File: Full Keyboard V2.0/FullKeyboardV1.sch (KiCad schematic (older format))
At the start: 210 parts, among them SW1 Esc, SW10 2, SW11 W, SW12 S, SW13 Z, SW15 3, SW16 E, SW17 D, SW18 X, SW19 4, SW2 Tab, SW20 R, SW21 F, SW22 C, SW23 5, SW24 T, SW25 G, SW26 V, SW27 6, SW28 Y, SW29 H, SW3 Caps, SW30 B, SW32 7, SW33 U, SW34 J, SW35 N, SW36 8, SW37 I, SW38 K, SW39 M, SW4 double_key, SW40 9, SW41 O, SW42 L, SW43 <, SW44 0, SW45 P, SW46 ;, SW47 >, SW49 Minus, SW5 End/Home, SW50 [, SW51 \", SW52 /, SW54 =, SW55 ], SW59 BKSPC, SW6 1, SW60 \\, SW61 Enter, SW63 Til, SW64 Del, SW65 Pg Up, SW66 Pg Dw, SW7 Q, SW8 A, SW9 double_key, U5 Cherry_bottom_row

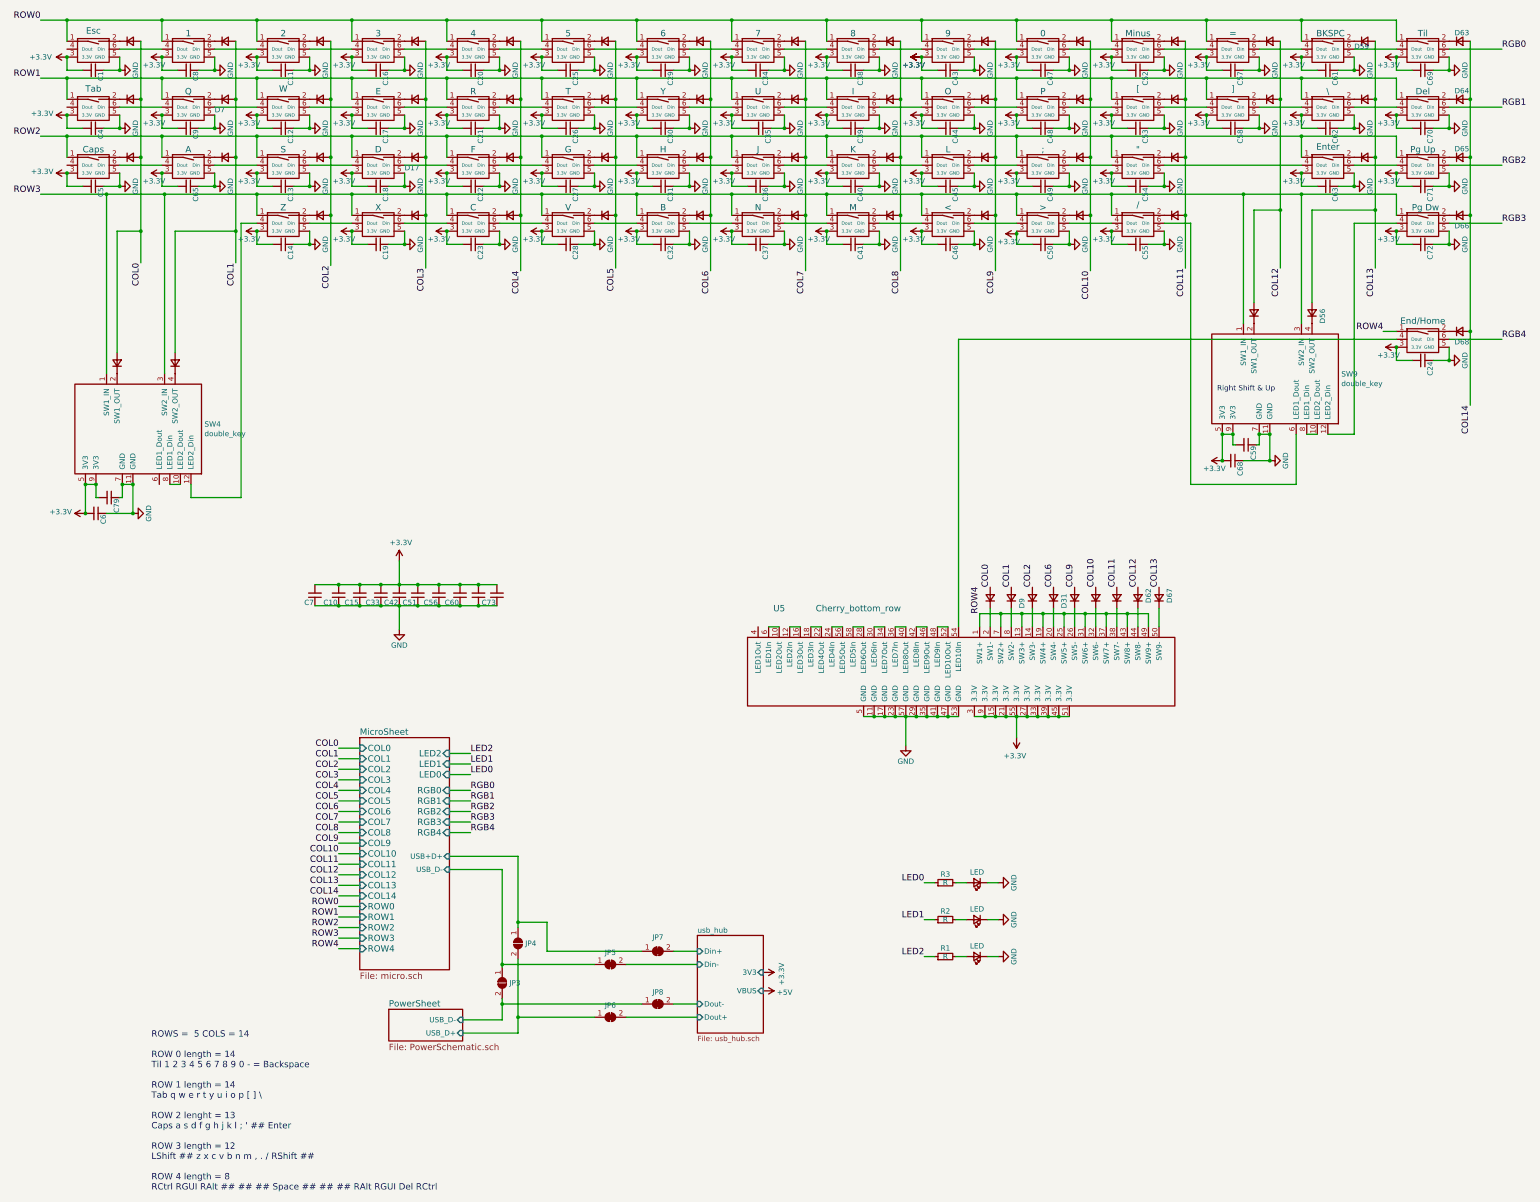
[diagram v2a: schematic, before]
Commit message: Added solder jumpers to allow for daisy chaining RGB rows
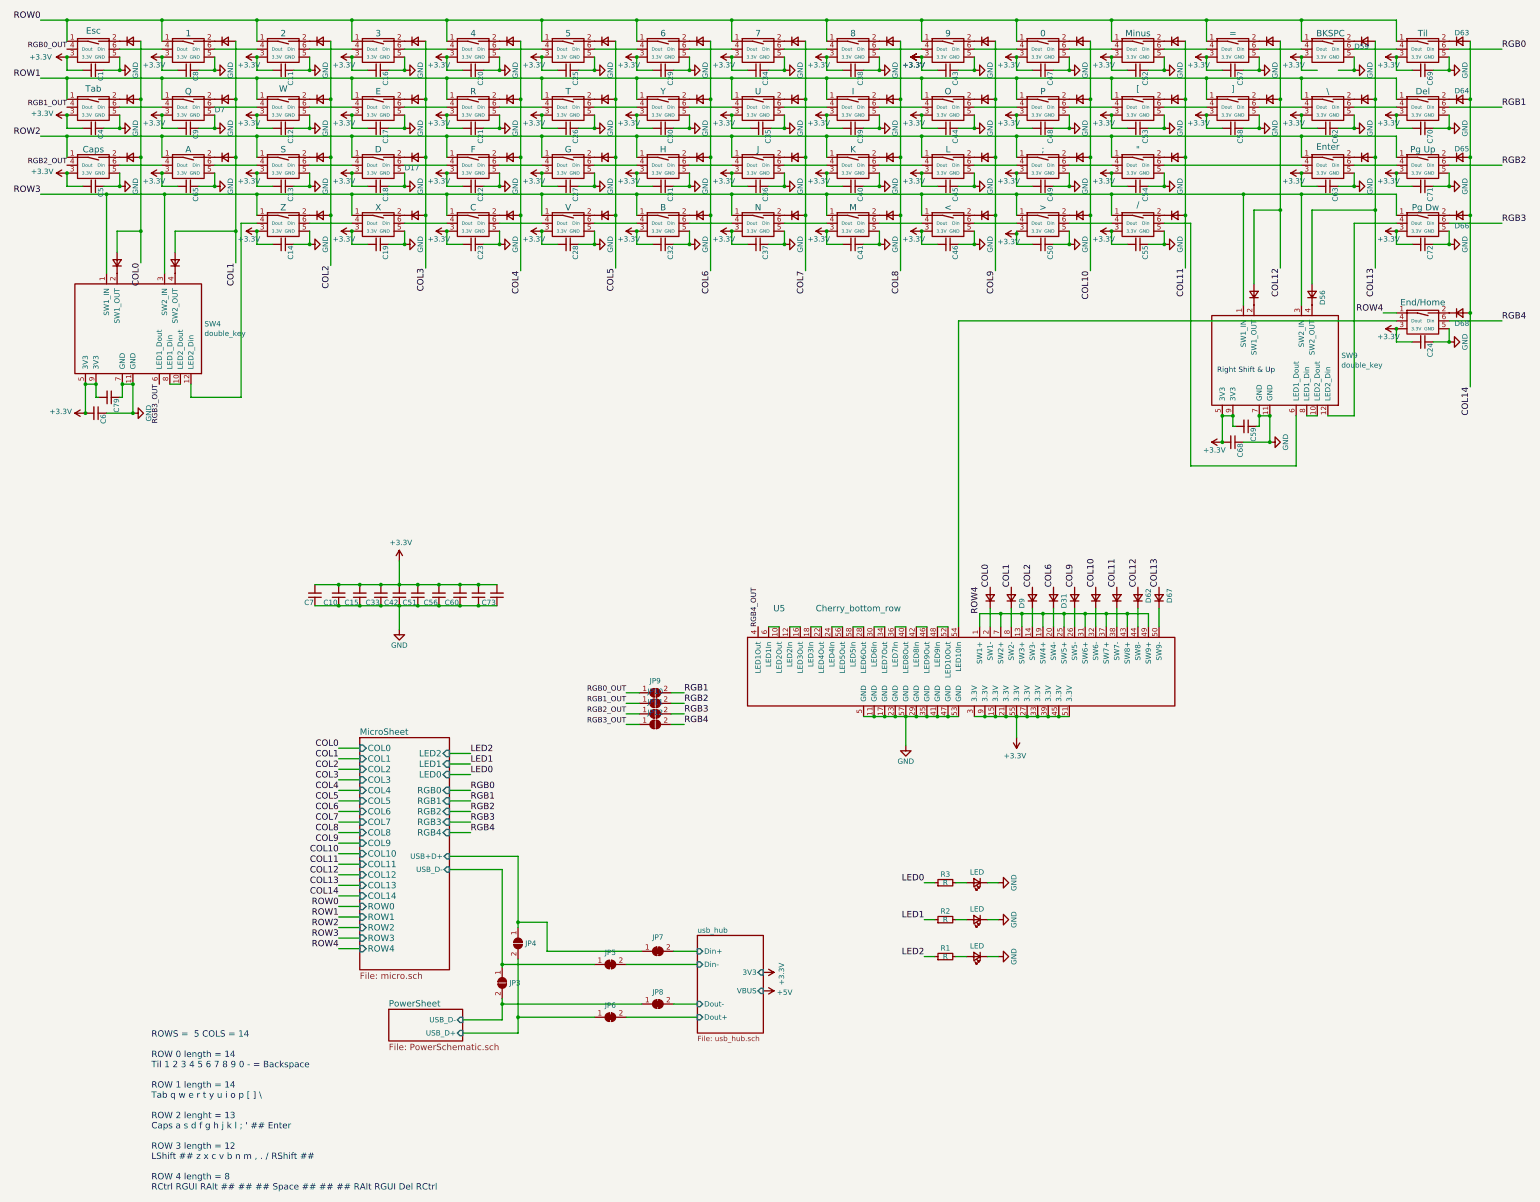
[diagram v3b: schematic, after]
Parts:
- removed C61: C_Small, Capacitor_SMD:C_0603_1608Metric, symbol Device:C_Small
- added JP10, JP11, JP12, JP9: SolderJumper_2_Open, Jumper:SolderJumper-2_P1.3mm_Open_RoundedPad1.0x1.5mm, symbol Jumper:SolderJumper_2_Open
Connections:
- net RGB1: now also JP9.2 (B)
- net RGB2: now also JP10.2 (B)
- net RGB3: now also JP11.2 (B)
- net RGB4: now also JP12.2 (B)
- net RGB0_OUT: now reaches SW1.4 (Dout)
- net RGB0_OUT: now also JP9.1 (A)
- net RGB1_OUT: now reaches SW2.4 (Dout)
- net RGB1_OUT: now also JP10.1 (A)
- net RGB2_OUT: now reaches SW3.4 (Dout)
- net RGB2_OUT: now also JP11.1 (A)
- net RGB4_OUT: now reaches U5.4 (LED1Out)
- net RGB3_OUT: now reaches SW4.6 (LED1_Dout)
- net RGB3_OUT: now also JP12.1 (A)
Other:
- moved on the sheet: C24, C59, C6, C68, C79, D56, D68, SW4, SW9
